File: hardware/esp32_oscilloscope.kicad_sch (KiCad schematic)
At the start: 7 parts, among them J1 Oled 1.3" I2C, J2 Vin, SW1 Pause_btn, U1 ESP32-WROOM-32

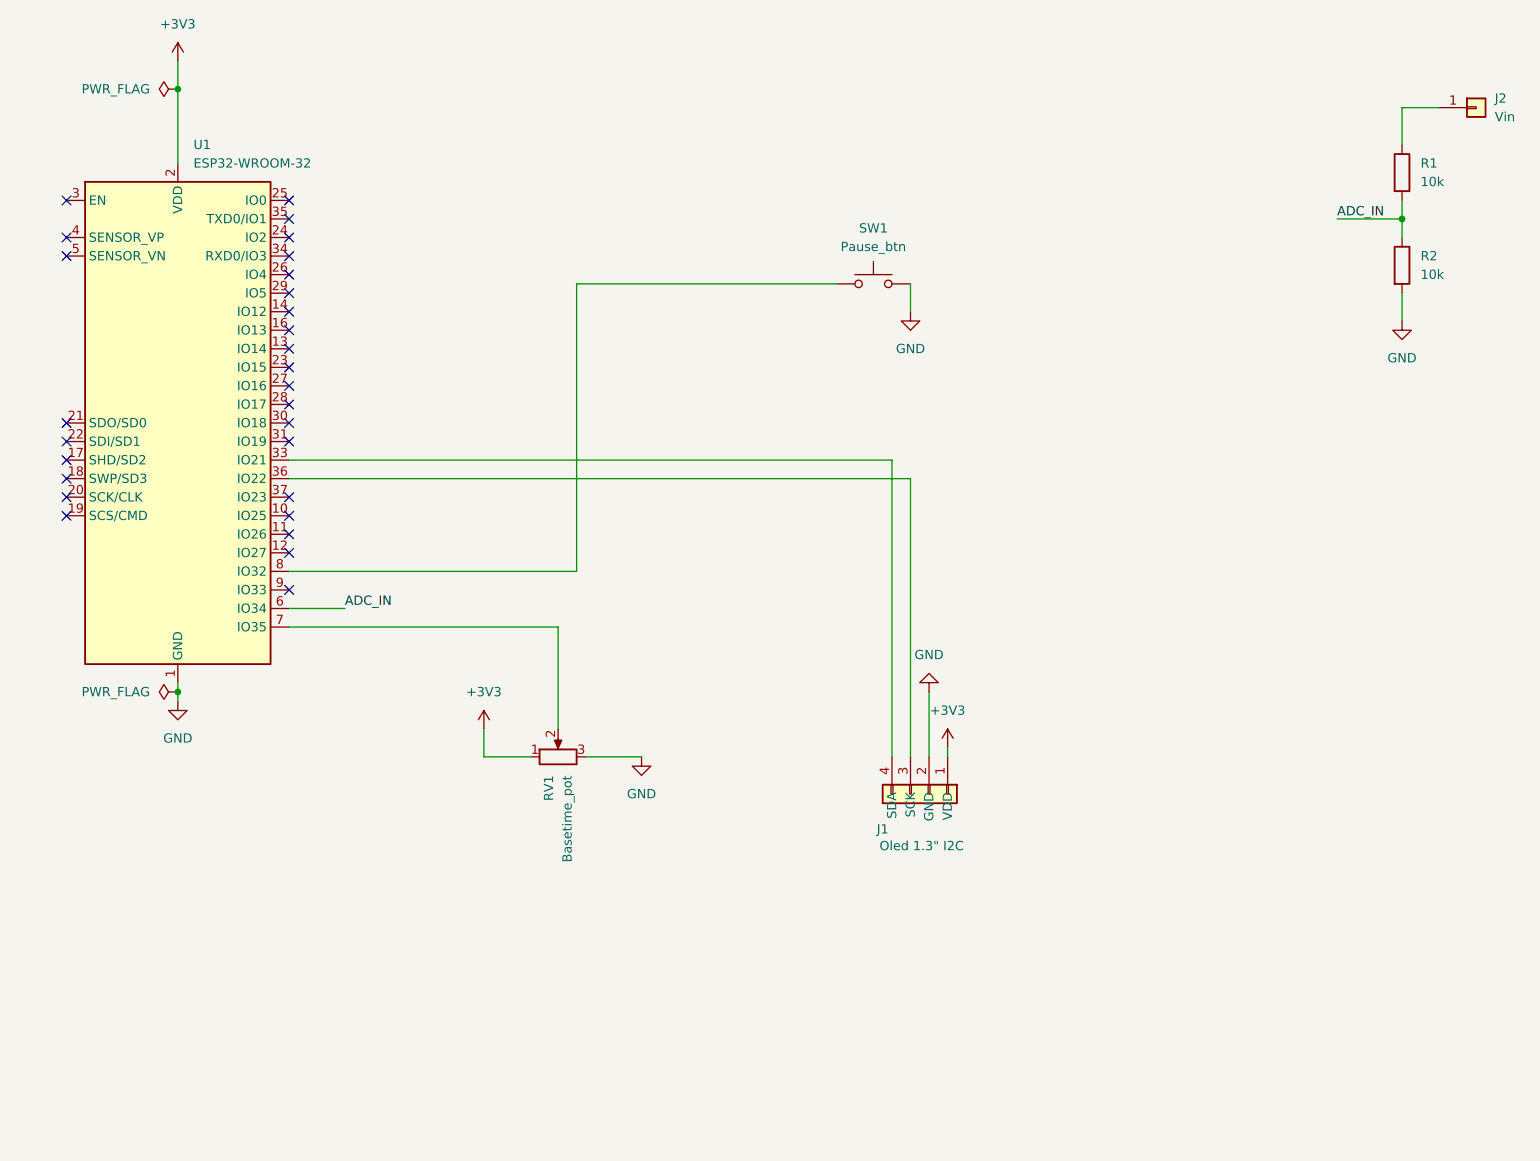
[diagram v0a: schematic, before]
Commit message: hardware: aggiornato schema elettrico per v1.1.0
Sostituito potenziometro analogico con encoder rotativo. Aggiunto connettore a 5 pin per modulo KY-040 ed esportato il nuovo schematic.png per il README.
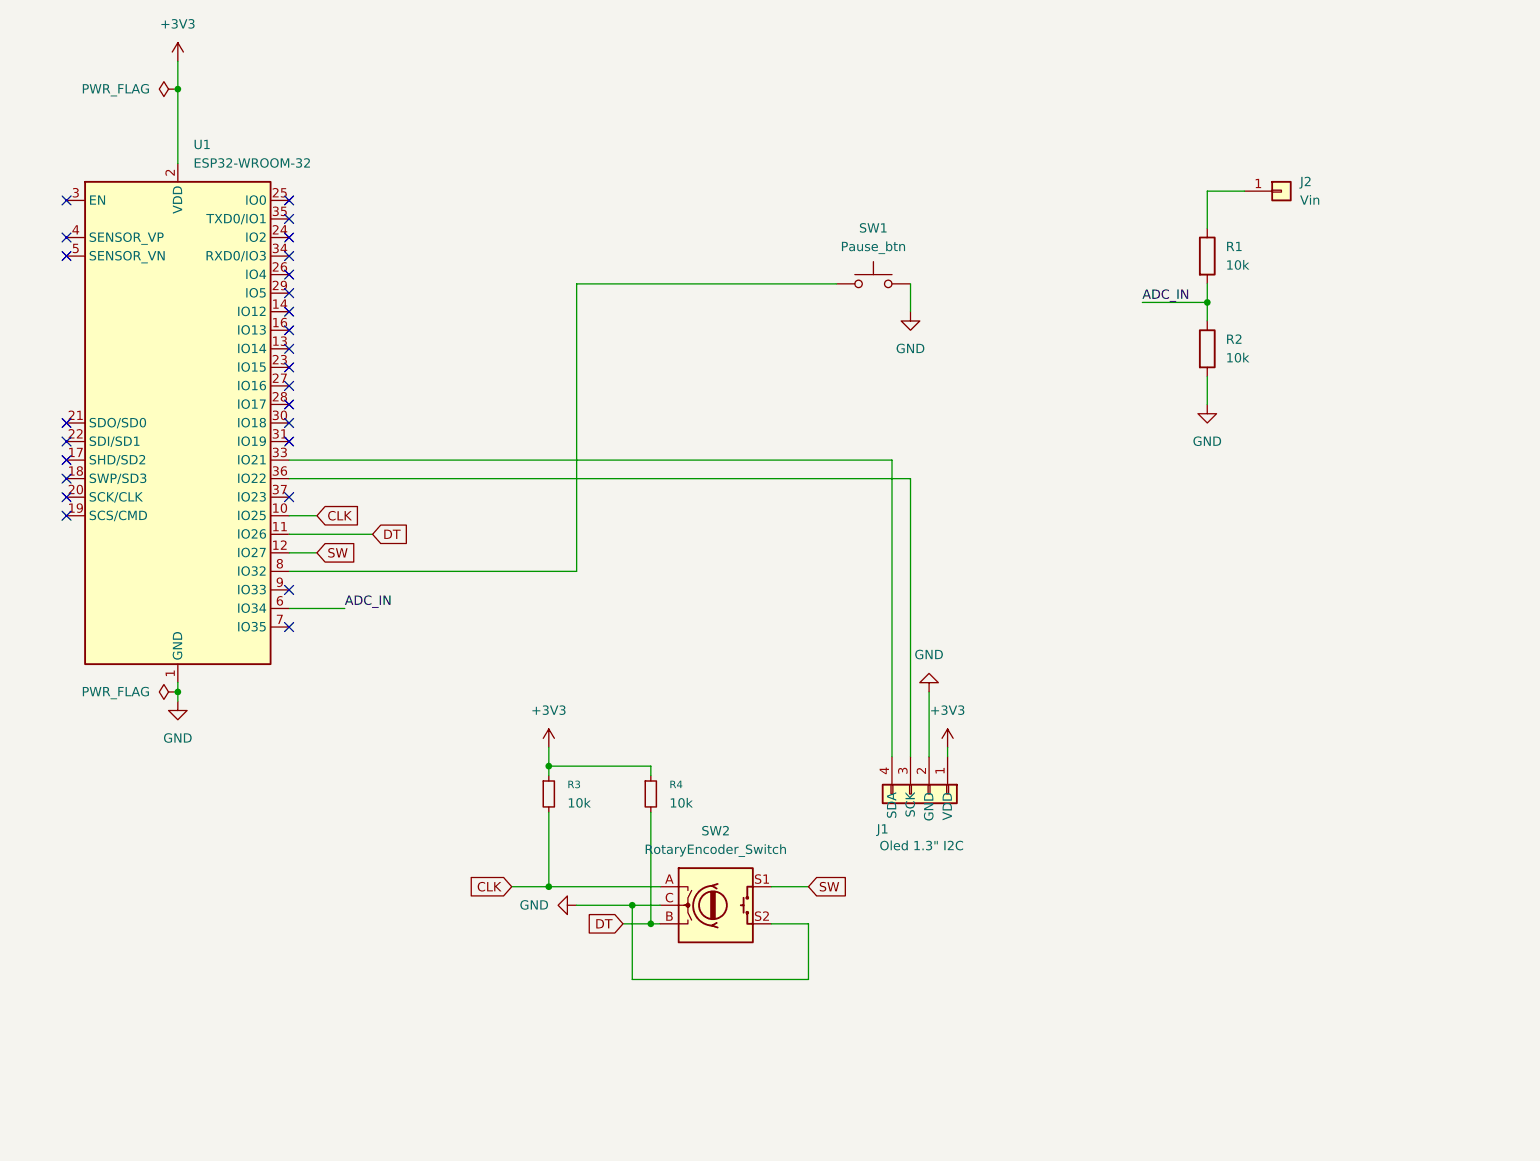
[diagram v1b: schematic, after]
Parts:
- removed RV1: Basetime_pot, symbol Device:R_Potentiometer
- added R3, R4: 10k, symbol Device:R_Small
- added SW2: RotaryEncoder_Switch, symbol Device:RotaryEncoder_Switch
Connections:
- net +3V3: now also R3.1, R4.1
- net GND: now also SW2.C, SW2.S2
- net CLK: now reaches U1.10 (IO25)
- net CLK: now also R3.2, SW2.A
- net DT: now reaches U1.11 (IO26)
- net DT: now also R4.2, SW2.B
- net SW: now reaches U1.12 (IO27)
- net SW: now also SW2.S1
- no-connect marks 28 -> 26
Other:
- moved on the sheet: J2, R1, R2

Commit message: Fix: Aggiornati schemi KiCad e pinout per la release v1.2.0
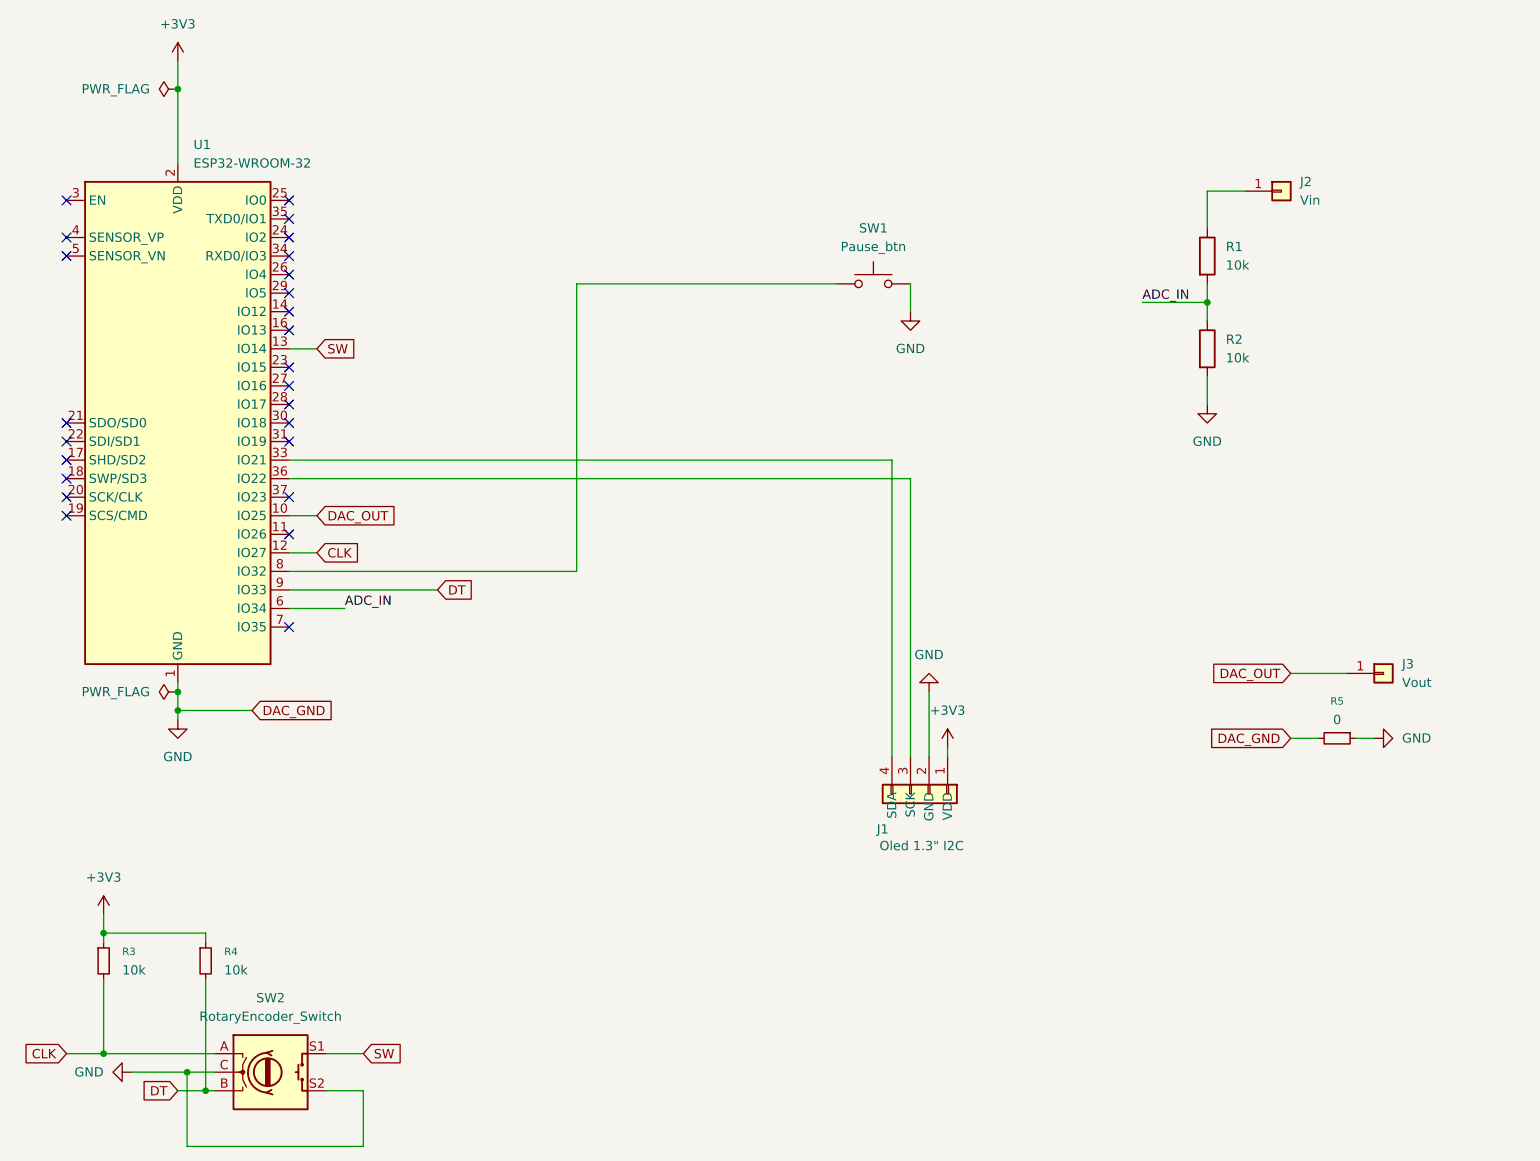
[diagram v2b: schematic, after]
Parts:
- added J3: Vout, symbol Connector_Generic:Conn_01x01
- added R5: 0, symbol Device:R_Small
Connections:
- net CLK: now also U1.12 (IO27); no longer U1.10 (IO25)
- net DT: now also U1.9 (IO33); no longer U1.11 (IO26)
- net GND: now also R5.1, R5.2
- net SW: now also U1.13 (IO14); no longer U1.12 (IO27)
- new net DAC_OUT: J3.1 (Pin_1), U1.10 (IO25)
- no-connect marks 26 -> 25
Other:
- moved on the sheet: R3, R4, SW2
